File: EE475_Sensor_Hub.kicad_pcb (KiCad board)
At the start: 2 copper layers, 38.1 x 53.3 mm, 5 parts, among them J1 Conn_01x04_Female, J2 Conn_01x04_Female, J3 Conn_01x15_Female, J4 Conn_01x15_Female

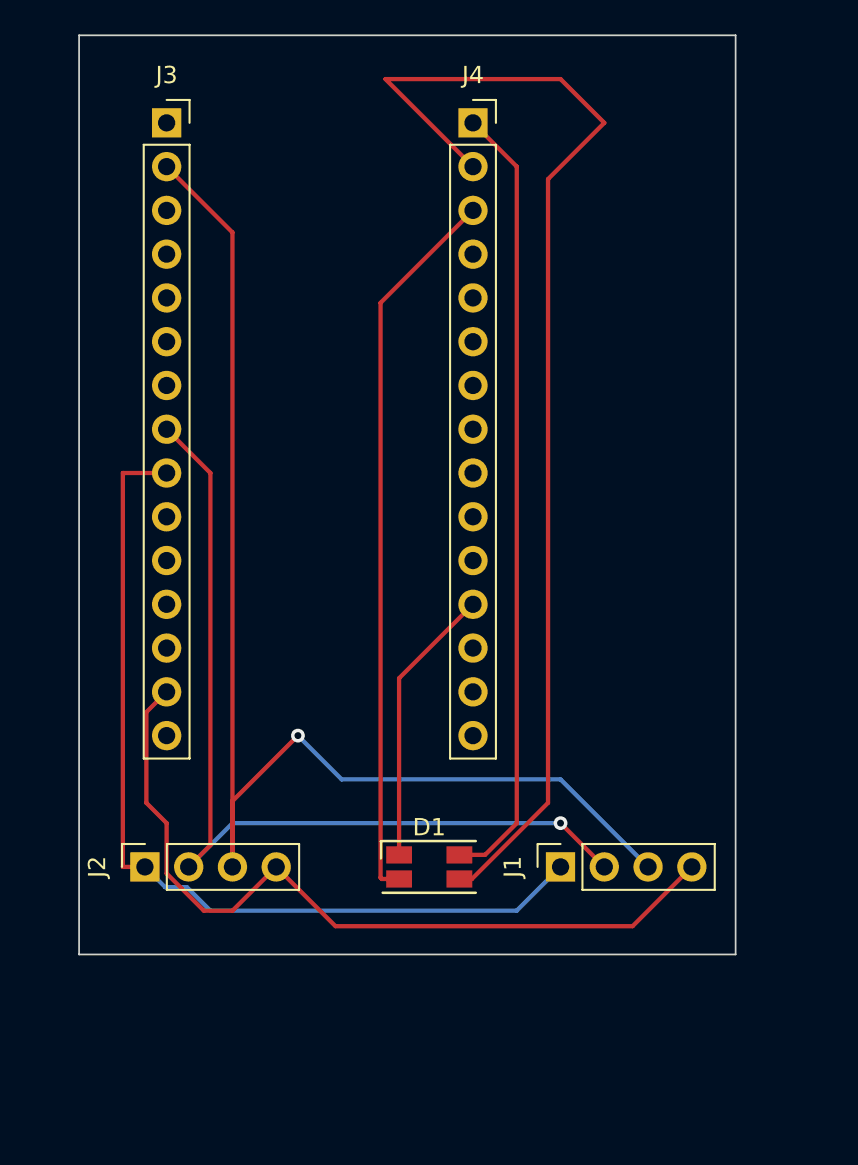
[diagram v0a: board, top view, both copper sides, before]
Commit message: Finish the PCB trace and pass the Design rule checker
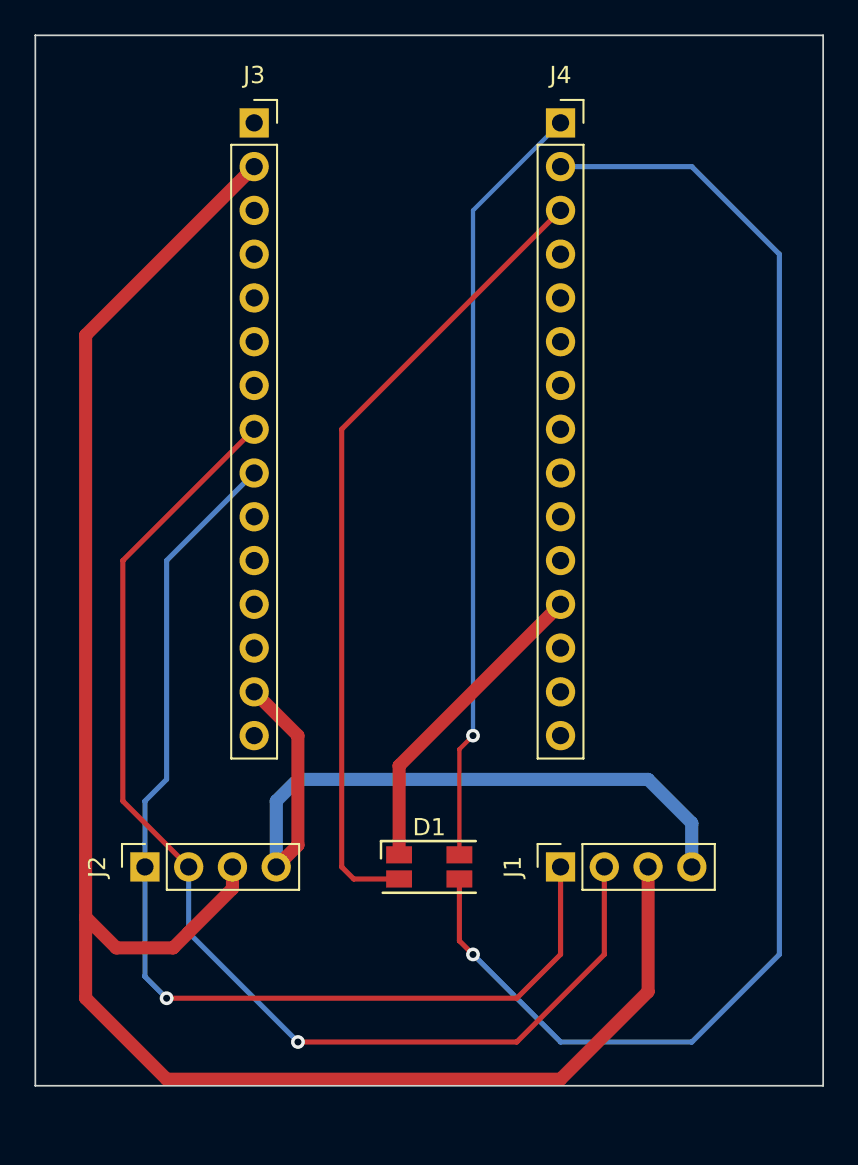
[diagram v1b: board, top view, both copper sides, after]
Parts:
- moved J3 5.08 mm to (129.5, 68.6)
- moved J4 5.08 mm to (147.3, 68.6)
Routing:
- net Net-(J1-Pad3): track 74.9 -> 108.2 mm, vias 1 -> 0
- net Net-(J1-Pad2): track 53.2 -> 67.9 mm
- net Net-(D1-Pad3): track 68.7 -> 82.1 mm, vias 0 -> 1
- net Net-(J1-Pad1): track 52.9 -> 62.6 mm, vias 0 -> 1
- net Net-(D1-Pad2): track 42.1 -> 47.0 mm
- net Net-(J1-Pad4): track 46.8 -> 43.8 mm
- net Net-(D1-Pad1): track 16.3 -> 18.4 mm
- net Net-(D1-Pad4): track 45.8 -> 44.9 mm, vias 0 -> 1
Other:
- board size 38.1 x 53.3 mm -> 45.7 x 61 mm

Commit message: Final design of the PCB baord for Sensor Controller
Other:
- board size 45.7 x 61 mm -> 45.7 x 63.5 mm
- board text added: "Sensor Controller"
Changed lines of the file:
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@@
     )
   )
-  (gr_line (start 116.84 124.46) (end 116.84 63.5) (layer "Edge.Cuts") (width 0.1))
-  (gr_line (start 162.56 124.46) (end 116.84 124.46) (layer "Edge.Cuts") (width 0.1))
-  (gr_line (start 162.56 63.5) (end 162.56 124.46) (layer "Edge.Cuts") (width 0.1))
+  (gr_line (start 116.84 127) (end 116.84 63.5) (layer "Edge.Cuts") (width 0.1))
+  (gr_line (start 162.56 127) (end 116.84 127) (layer "Edge.Cuts") (width 0.1))
+  (gr_line (start 162.56 63.5) (end 162.56 127) (layer "Edge.Cuts") (width 0.1))
   (gr_line (start 116.84 63.5) (end 162.56 63.5) (layer "Edge.Cuts") (width 0.1))
+  (gr_text "Sensor Controller" (at 154.94 88.9 90) (layer "F.SilkS")
+    (effects (font (size 2 2) (thickness 0.3)))
+  )
   (segment (start 137.95 105.89) (end 147.32 96.52) (width 0.76) (layer "F.Cu") (net 1))
   (segment (start 137.95 111.06) (end 137.95 105.89) (width 0.76) (layer "F.Cu") (net 1))

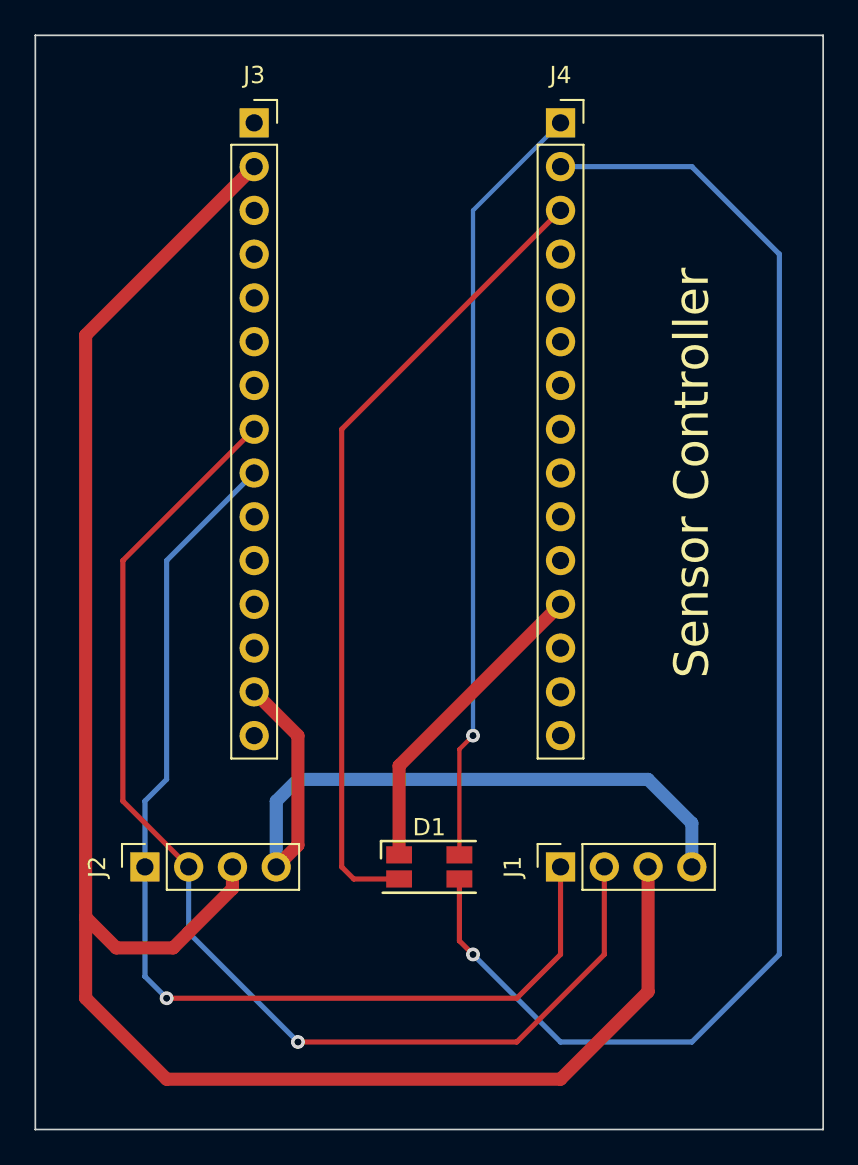
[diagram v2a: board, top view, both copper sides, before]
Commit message: Updated version of the PCB based on professor and TAs feedback
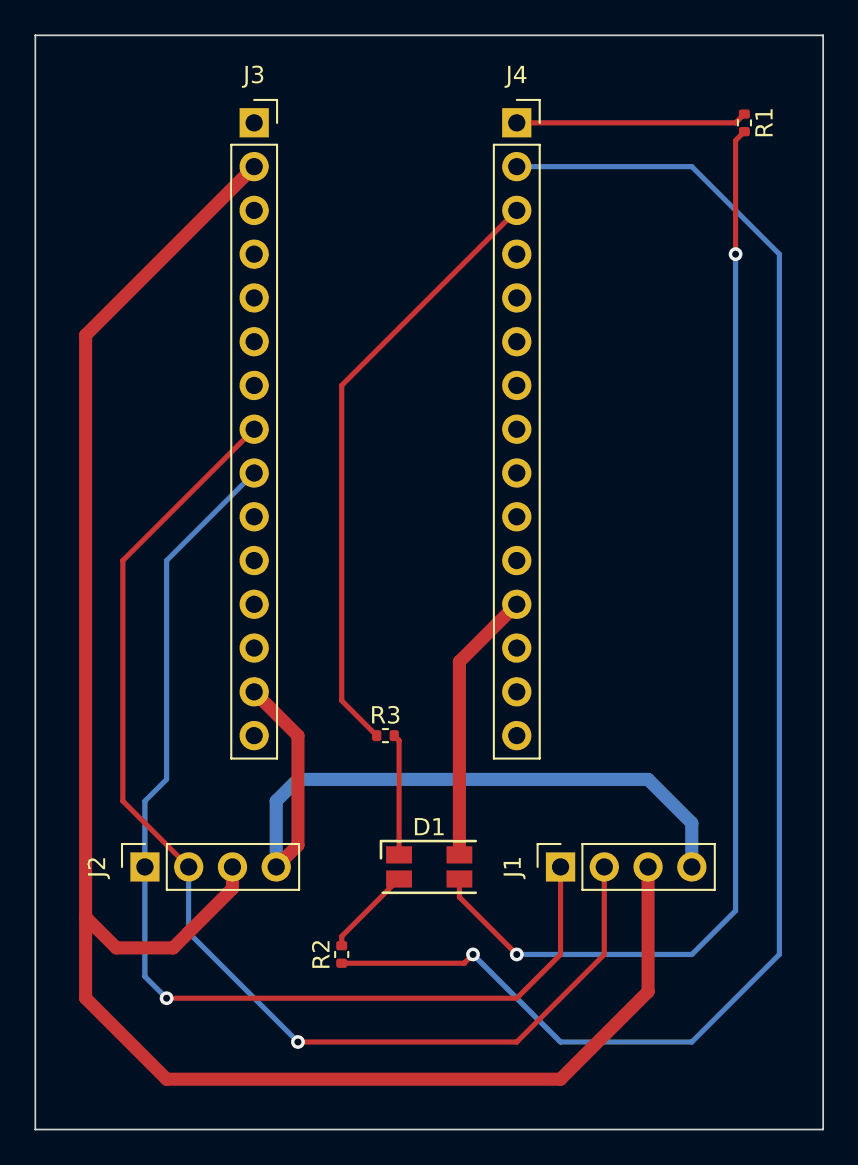
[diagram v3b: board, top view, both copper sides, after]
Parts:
- added R1: 1k, Resistor_SMD:R_0402_1005Metric, F.Cu at (158.0, 68.6)
- added R2: 1k, Resistor_SMD:R_0402_1005Metric, F.Cu at (134.6, 116.8)
- added R3: 1k, Resistor_SMD:R_0402_1005Metric, F.Cu at (137.2, 104.1)
- D1: value LED_ABGR -> LED_BGRK
- moved J4 2.54 mm to (144.8, 68.6)
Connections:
- D1 pad 1: Net-(D1-Pad1) -> Net-(R3-Pad2)
- D1 pad 2: Net-(D1-Pad2) -> Net-(R2-Pad2)
- D1 pad 3: Net-(D1-Pad3) -> Net-(R1-Pad2)
- D1 pad 4: Net-(D1-Pad4) -> Net-(J4-Pad12)
- J4 pad 1: Net-(D1-Pad4) -> Net-(J4-Pad1)
- J4 pad 12: Net-(D1-Pad1) -> Net-(J4-Pad12)
- J4 pad 2: Net-(D1-Pad3) -> Net-(J4-Pad2)
- J4 pad 3: Net-(D1-Pad2) -> Net-(J4-Pad3)
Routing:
- net Net-(J4-Pad2): track 0.00 -> 87.8 mm, vias 0 -> 1
- net Net-(D1-Pad3): track 82.1 -> 0.00 mm, vias 1 -> 0
- net Net-(R1-Pad2): track 0.00 -> 64.9 mm, vias 0 -> 2
- net Net-(D1-Pad2): track 47.0 -> 0.00 mm
- net Net-(D1-Pad4): track 44.9 -> 0.00 mm, vias 1 -> 0
- net Net-(J4-Pad3): track 0.00 -> 35.5 mm
- net Net-(D1-Pad1): track 18.4 -> 0.00 mm
- net Net-(J4-Pad12): track 0.00 -> 15.9 mm
- net Net-(J4-Pad1): track 0.00 -> 13.4 mm
- net Net-(R3-Pad2): track 0.00 -> 7.04 mm
- net Net-(R2-Pad2): track 0.00 -> 5.25 mm
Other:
- board text removed: "Sensor Controller"

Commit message: Modify LED and resistor footprint
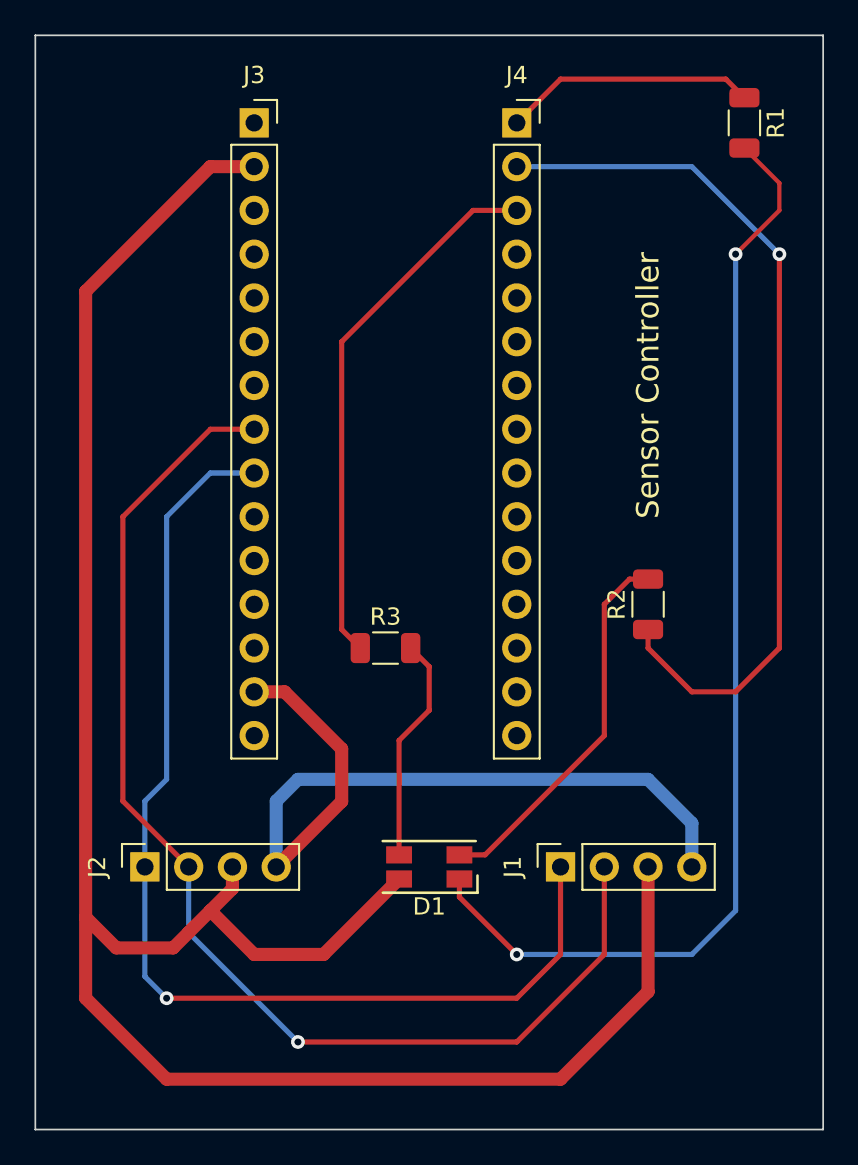
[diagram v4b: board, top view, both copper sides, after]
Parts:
- D1: value LED_BGRK -> LED_RGBA
- R1, R2, R3: footprint Resistor_SMD:R_0402_1005Metric -> Resistor_SMD:R_1206_3216Metric
- moved R2 27.0 mm to (152.4, 96.5)
- moved R3 5.08 mm to (137.2, 99.1)
- turned D1 to 180 degrees
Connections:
- D1 pad 1: Net-(R3-Pad2) -> Net-(D1-Pad1)
- D1 pad 3: Net-(R1-Pad2) -> Net-(D1-Pad3)
- D1 pad 4: Net-(J4-Pad12) -> Net-(D1-Pad4)
- J1 pad 3: Net-(J1-Pad3) -> Net-(D1-Pad4)
- J2 pad 3: Net-(J1-Pad3) -> Net-(D1-Pad4)
- J3 pad 2: Net-(J1-Pad3) -> Net-(D1-Pad4)
- J4 pad 12: Net-(J4-Pad12) -> unconnected-(J4-Pad12)
- R1 pad 2: Net-(R1-Pad2) -> Net-(D1-Pad1)
- R3 pad 2: Net-(R3-Pad2) -> Net-(D1-Pad3)
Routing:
- net Net-(D1-Pad4): track 0.00 -> 123.9 mm
- net Net-(J1-Pad3): track 108.2 -> 0.00 mm
- net Net-(D1-Pad1): track 0.00 -> 65.7 mm, vias 0 -> 2
- net Net-(R1-Pad2): track 64.9 -> 0.00 mm, vias 2 -> 0
- net Net-(J4-Pad2): track 87.8 -> 51.0 mm
- net Net-(D1-Pad2): track 5.25 -> 22.0 mm
- net Net-(J4-Pad12): track 15.9 -> 0.00 mm
- net Net-(D1-Pad3): track 0.00 -> 13.2 mm
- net Net-(R3-Pad2): track 7.04 -> 0.00 mm
- net Net-(J4-Pad3): track 35.5 -> 31.5 mm
- net Net-(J1-Pad4): track 43.8 -> 46.9 mm
- net Net-(J1-Pad1): track 62.6 -> 64.1 mm
- net Net-(J1-Pad2): track 67.9 -> 69.4 mm
- net Net-(J4-Pad1): track 13.4 -> 14.7 mm
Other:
- board text added: "Sensor Controller"
